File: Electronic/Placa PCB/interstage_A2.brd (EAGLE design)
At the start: 82.5 x 29 mm, 9 parts, among them J1 0532611271, J3 0532611271, Q1 PMV16XNR, U1 LM70CIMM-3, U2 LM70CIMM-3

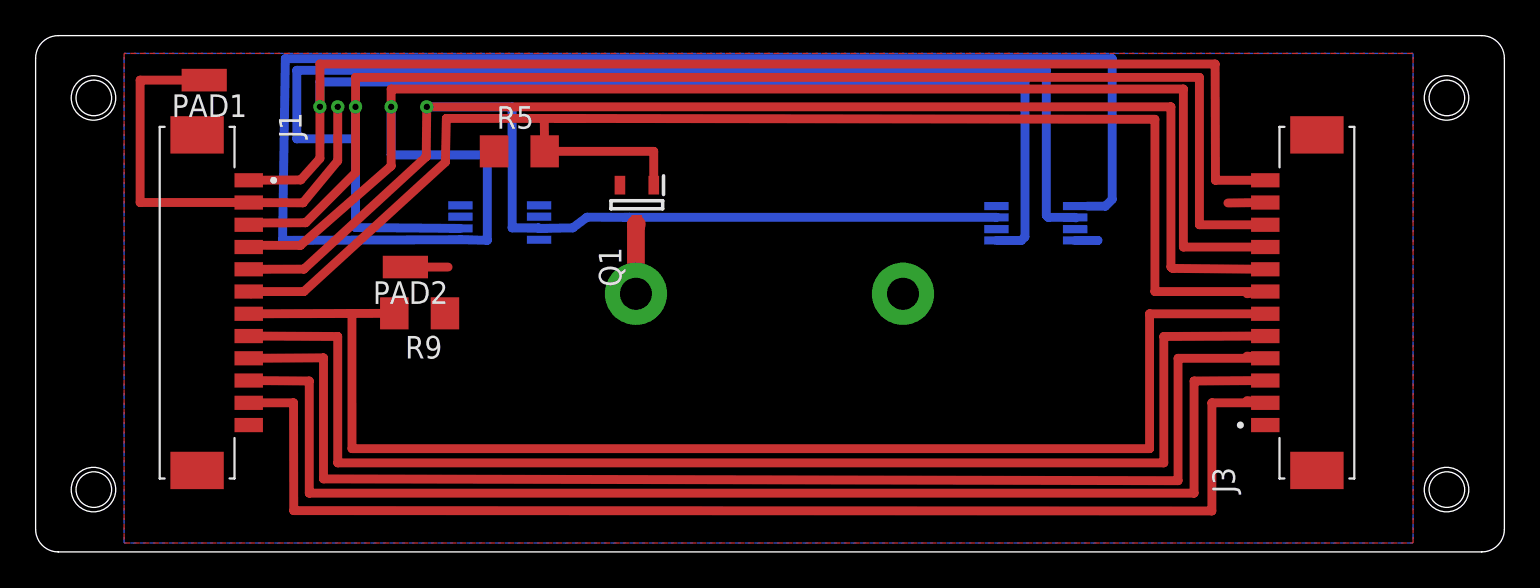
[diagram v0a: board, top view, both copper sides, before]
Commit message: Ensamblaje placa
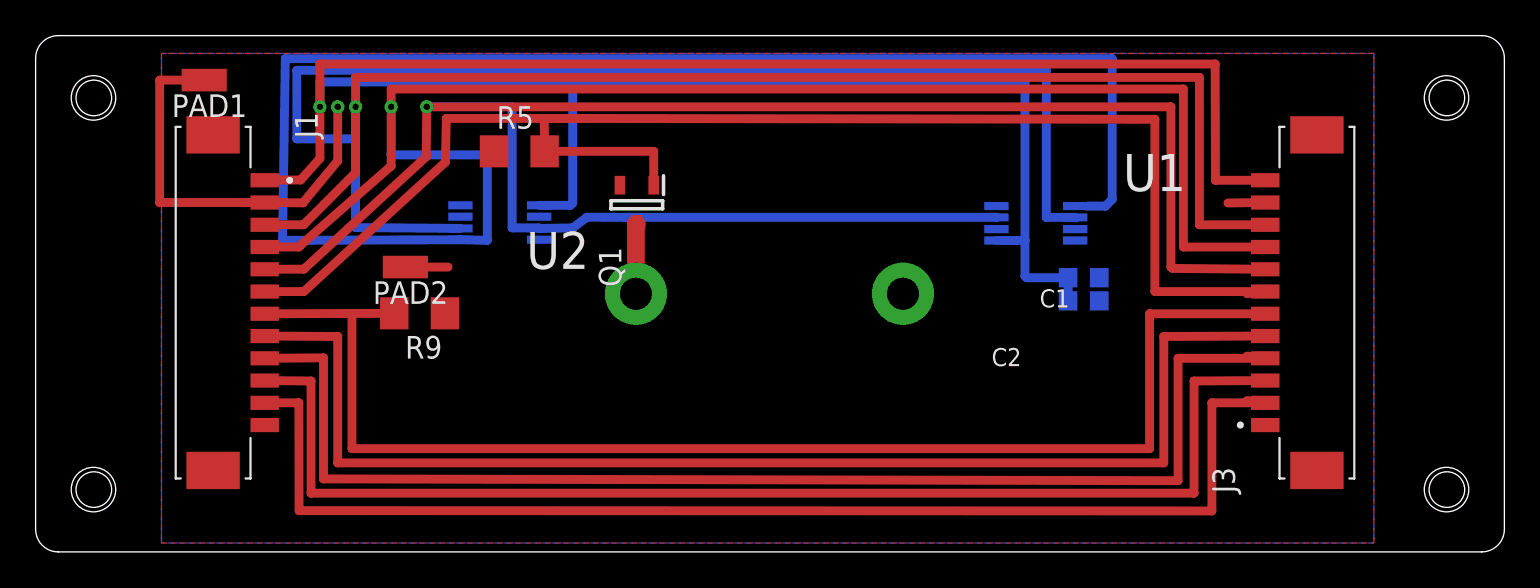
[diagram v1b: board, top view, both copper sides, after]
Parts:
- added C1, C2: 0.1pF, rcl:C0603K
- moved J1 0.90 mm to (10.0, 14.0)
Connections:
- net GND: now also C1.2, C2.2
- net VCC: now also C1.1, C2.1
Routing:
- net VCC: track 120.8 -> 134.6 mm
- net GND: track 31.5 -> 29.8 mm
- net MISO: track 162.7 -> 161.6 mm
- net OC1A: track 85.5 -> 84.4 mm
- net AIN0: track 71.5 -> 70.4 mm
- net INT0: track 69.7 -> 68.8 mm
- net MOSI: track 110.7 -> 109.8 mm
- net AIN1: track 74.6 -> 73.7 mm
- net T1: track 71.8 -> 70.9 mm
- net T0: track 70.3 -> 69.4 mm
- net SCK: track 143.7 -> 142.9 mm
